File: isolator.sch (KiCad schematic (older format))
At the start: 21 parts, among them U101 NE5532

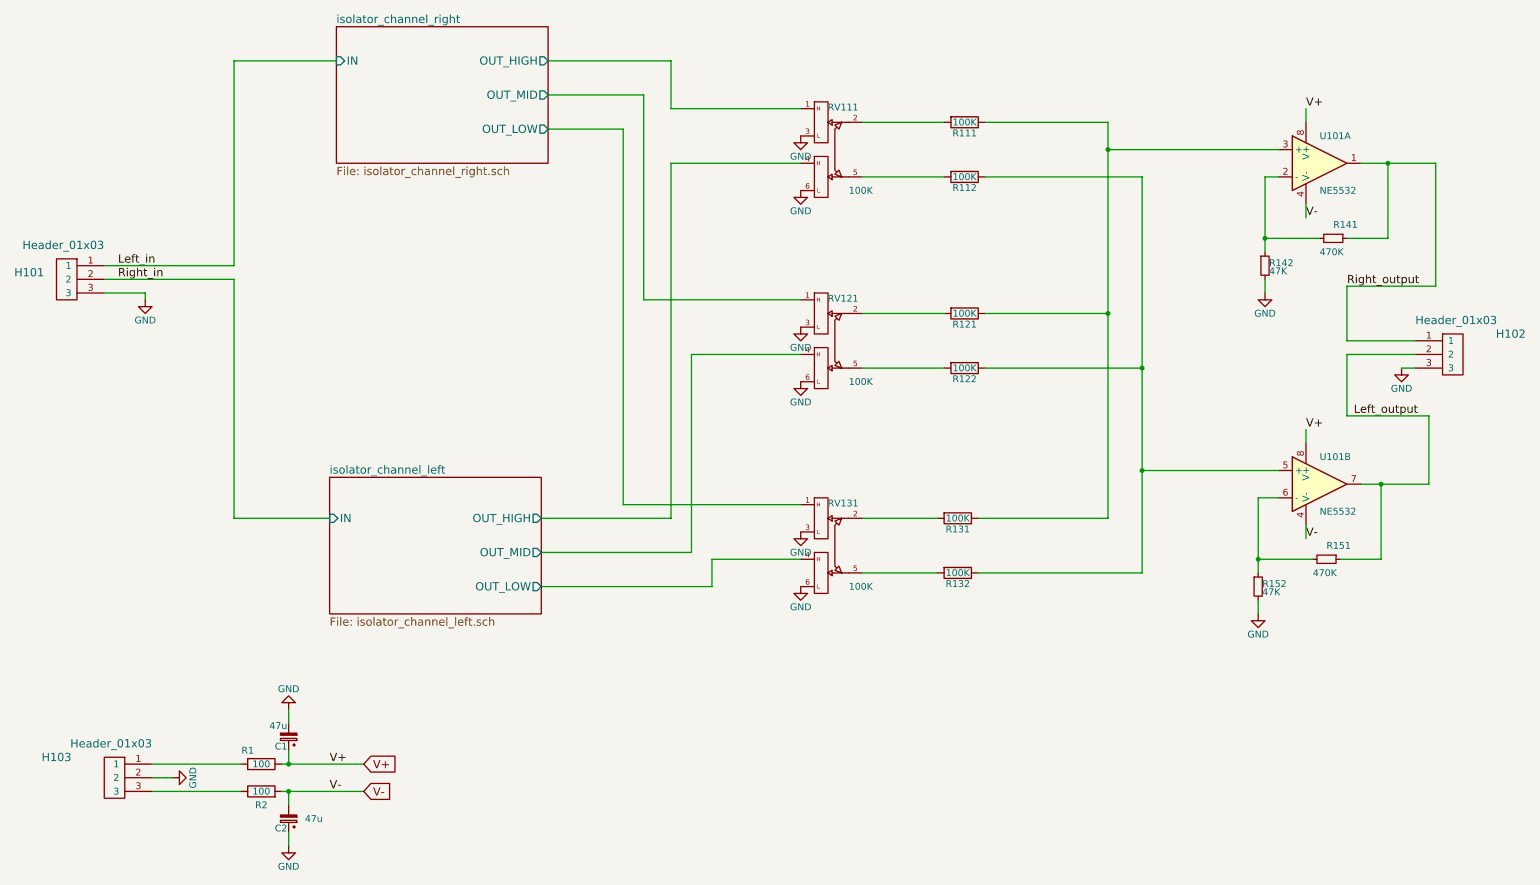
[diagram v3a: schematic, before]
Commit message: Updated components references and properties
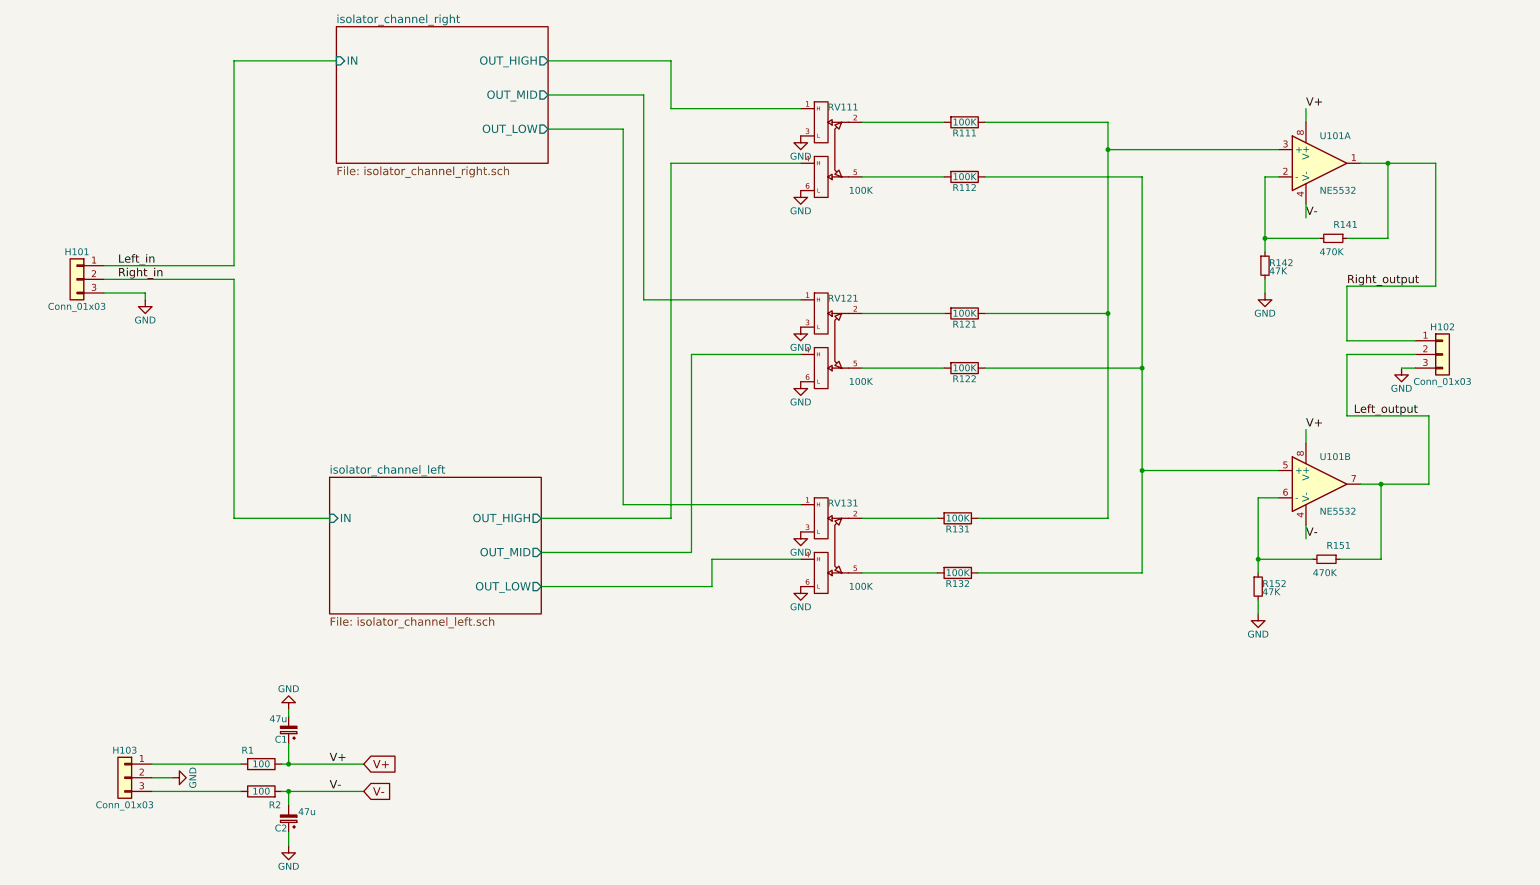
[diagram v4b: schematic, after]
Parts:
- removed H101, H102, H103: Header_01x03, Pin_Headers:Pin_Header_Angled_1x03, symbol Header_01x03
- added H101, H102, H103: Conn_01x03, Pin_Headers:Pin_Header_Angled_1x03_Pitch2.54mm, symbol Conn_01x03
- C1, C2: Description (none) -> Condensateurs électrolytiques aluminium – traversant 63volt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; Distributor (none) -> Mouser; Distributor Part # (none) -> 647-UVZ1J470MED; Manufacturer (none) -> Nichicon; Mfg_Part_# (none) -> UVZ1J470MED; Package (none) -> 2-THT
- R1, R2: footprint Resistors_ThroughHole:Resistor_Horizontal_RM7mm -> Resistors_THT:R_Axial_DIN0207_L6.3mm_D2.5mm_P10.16mm_Horizontal; Description (none) -> Résistances à couche métallique - Trou traversant 0.6W 1% 1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; Distributor (none) -> Mouser; Distributor Part # (none) -> 603-MF0207FTE52-100R; Manufacturer (none) -> Yageo; Mfg_Part_# (none) -> MF0207FTE52-100R; Mfg_Part_No CCF50100RFKR36 -> MF0207FTE52-100R; Package (none) -> DIN0204
- R141, R151: Description (none) -> Résistances à couche métallique - Trou traversant 470K OHM 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; Distributor (none) -> Mouser; Distributor Part # (none) -> 603-MFR-12FTF52-470K; Manufacturer (none) -> Yageo; Mfg_Part_# (none) -> MFR-12FTF52-470K; Mfg_Part_No CCF07470KGKE36 -> MFR-12FTF52-470K; Package (none) -> DIN0204
- R142, R152: Description (none) -> Résistances à couche métallique - Trou traversant 47K OHM 1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; Distributor (none) -> Mouser; Distributor Part # (none) -> 71-CCF0747K0JKE36; Manufacturer (none) -> Yageo; Mfg_Part_# (none) -> MFR-12FTF52-47K; Mfg_Part_No CCF0747K0JKE36 -> MFR-12FTF52-47K; Package (none) -> DIN0204
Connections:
- net GND: now also H101.3 (Pin_3), H102.3 (Pin_3), H103.2 (Pin_2)
- net Left_in: now also H101.1 (Pin_1)
- net Left_output: now also H102.2 (Pin_2)
- net Right_in: now also H101.2 (Pin_2)
- net Right_output: now also H102.1 (Pin_1)
- net at R1.2: now also H103.1 (Pin_1)
- net at R2.1: now also H103.3 (Pin_3)
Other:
- moved on the sheet: C1

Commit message: minor components edits
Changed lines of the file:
@@
 	7650 2450 8800 2450
 Wire Wire Line
-	8800 2450 8800 3850
-Wire Wire Line
-	8800 3850 8800 4600
-Wire Wire Line
-	8800 4600 8800 5350
+	8800 2450 8800 5350
 Wire Wire Line
 	8800 3850 7650 3850
@@
 	8550 4950 7600 4950
 Wire Wire Line
-	8550 2050 8550 2250
-Wire Wire Line
-	8550 2250 8550 3450
-Wire Wire Line
-	8550 3450 8550 4950
+	8550 2050 8550 4950
 Wire Wire Line
 	8550 3450 7650 3450
@@
 	9800 2450 9700 2450
 Wire Wire Line
-	9700 2450 9700 2900
-Wire Wire Line
-	9700 2900 9700 3000
+	9700 2450 9700 3000
 Wire Wire Line
 	10100 2900 9700 2900
 Connection ~ 9700 2900
 Wire Wire Line
-	10400 2350 10600 2350
-Wire Wire Line
-	10600 2350 10950 2350
+	10400 2350 10950 2350
 Wire Wire Line
 	10600 2350 10600 2900
@@
 	9700 3300 9700 3200
 Wire Wire Line
-	9650 4800 9650 5250
-Wire Wire Line
-	9650 5250 9650 5350
+	9650 4800 9650 5350
 Wire Wire Line
 	10050 5250 9650 5250
@@
 	9800 4800 9650 4800
 Wire Wire Line
-	10400 4700 10550 4700
-Wire Wire Line
-	10550 4700 10900 4700
+	10400 4700 10900 4700
 $Comp
 L GND #PWR010
@@
 $EndComp
 Wire Wire Line
-	2500 6750 2550 6750
-Wire Wire Line
-	2550 6750 3100 6750
+	2500 6750 3100 6750
 Wire Wire Line
 	2550 6750 2550 6600
 Connection ~ 2550 6750
 Wire Wire Line
-	2500 6950 2550 6950
-Wire Wire Line
-	2550 6950 3100 6950
+	2500 6950 3100 6950
 Wire Wire Line
 	2550 7050 2550 6950
